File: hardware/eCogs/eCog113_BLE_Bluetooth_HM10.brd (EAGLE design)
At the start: 47.5 x 28 mm, 5 parts

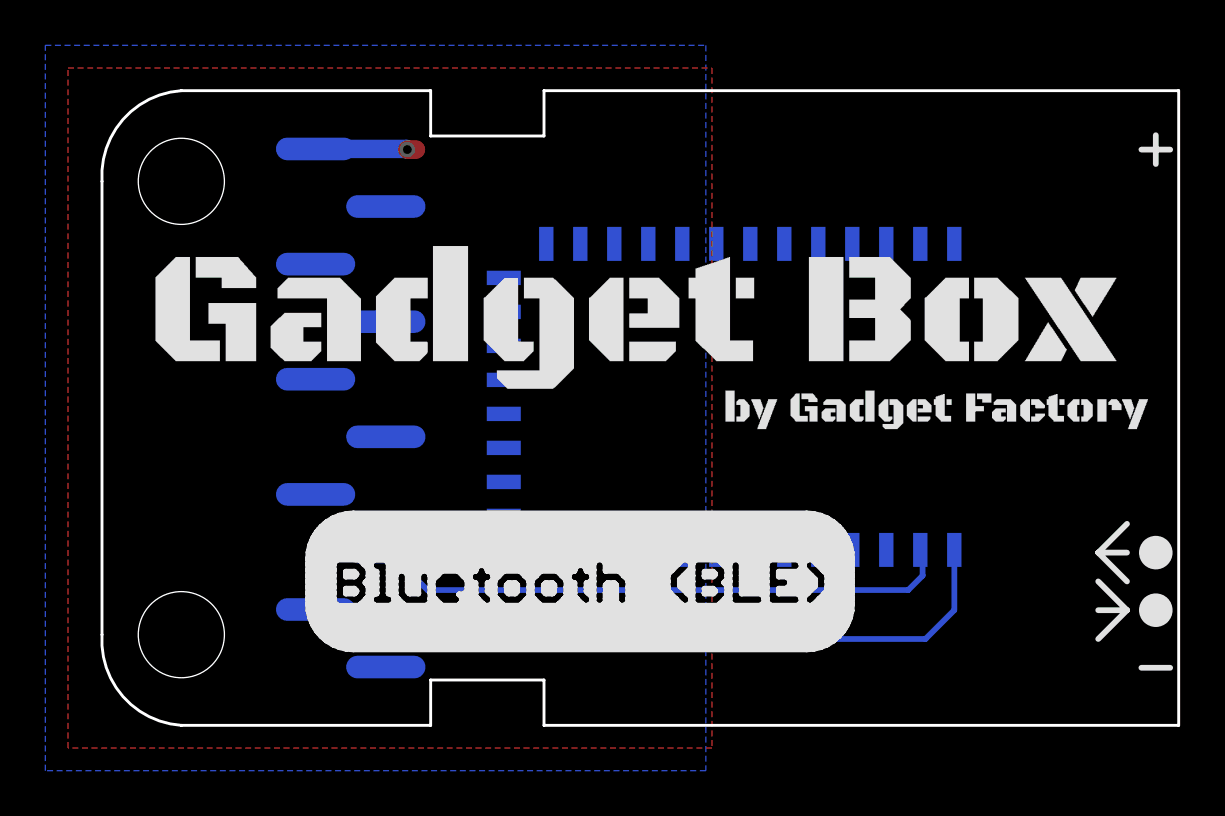
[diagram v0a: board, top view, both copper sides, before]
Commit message: Update eCogs to through hole
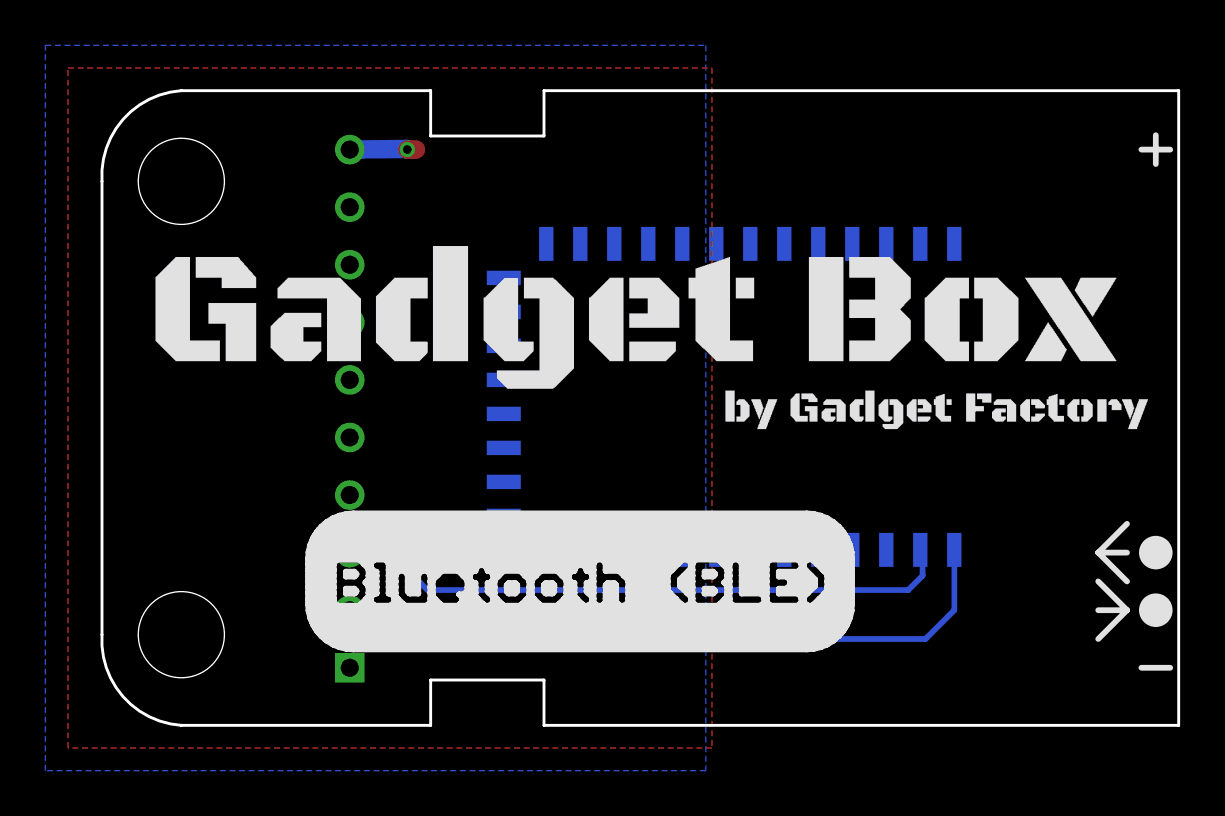
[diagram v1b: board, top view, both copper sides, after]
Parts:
- ECOG: value ECOG_GENERAL_ROWECOG_GENERAL_SMD -> ECOG_GENERAL_ROWTHROUGHOLE; device eCogs:ECOG_GENERAL_SMD -> eCogs:ECOG_GENERAL_TH
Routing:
- net RX/MOSI: track 25.8 -> 27.4 mm
- net 3V3: track 7.62 -> 6.12 mm
- net TX/MISO: track 31.9 -> 30.4 mm
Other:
- board text added: "ecog113 v2.1"
- board text removed: "ecog113 v2.0"
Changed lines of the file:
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@@
 <plain>
 <text x="40.099" y="25.273" size="0.8128" layer="22" font="vector" rot="MR0">ecog113.GadgetFactory.net</text>
-<text x="39.702" y="2.159" size="1.016" layer="22" font="vector" rot="MR0">ecog113 v2.0</text>
+<text x="39.702" y="2.159" size="1.016" layer="22" font="vector" rot="MR0">ecog113 v2.1</text>
 <text x="39.702" y="3.429" size="1.016" layer="22" font="vector" rot="MR0">BLE Bluetooth (HM-10)</text>
 <text x="39.702" y="4.699" size="1.016" layer="22" font="vector" rot="MR0">eCogs</text>
@@
 </autorouter>
 <elements>
-<element name="ECOG" library="eCogs" package="ECOG_GENERAL_SMD" value="ECOG_GENERAL_ROWECOG_GENERAL_SMD" x="0" y="0" smashed="yes">
-<attribute name="DIGIKEY" value="S1013EC-10-ND" x="0" y="0" size="1.778" layer="27" display="off"/>
-</element>
+<element name="ECOG" library="eCogs" package="ECOG_GENERAL_TH" value="ECOG_GENERAL_ROWTHROUGHOLE" x="0" y="0" smashed="yes"/>
 <element name="U$1" library="GadgetFactory" package="GADGETBOX_TEXT" value="" x="24.13" y="17.78"/>
 <element name="U$2" library="eCogs" package="LEGEND_DIO" value="" x="46.99" y="7.62"/>
@@
 <contactref element="E1" pad="11"/>
 <wire x1="21.6" y1="7.74" x2="23.1" y2="7.74" width="0.3048" layer="16"/>
-<wire x1="9.92324375" y1="25.429" x2="13.941" y2="25.429" width="0.8128" layer="16"/>
+<wire x1="11.43" y1="25.4" x2="13.941" y2="25.429" width="0.8128" layer="16"/>
 <wire x1="13.941" y1="25.429" x2="13.97" y2="25.4" width="0.8128" layer="16"/>
 <via x="13.97" y="25.4" extent="1-16" drill="0.381"/>
@@
 <contactref element="E1" pad="2"/>
 <contactref element="ECOG" pad="G1"/>
-<wire x1="13.02204375" y1="7.649" x2="13.179" y2="7.649" width="0.254" layer="16"/>
+<wire x1="11.43" y1="7.62" x2="13.179" y2="7.649" width="0.254" layer="16"/>
 <wire x1="13.179" y1="7.649" x2="14.859" y2="5.969" width="0.254" layer="16"/>
 <wire x1="14.859" y1="5.969" x2="36.068" y2="5.969" width="0.254" layer="16"/>
@@
 <contactref element="E1" pad="1"/>
 <contactref element="ECOG" pad="G0"/>
-<wire x1="9.92324375" y1="5.1110625" x2="12.6689375" y2="5.1110625" width="0.254" layer="16"/>
+<wire x1="11.43" y1="5.08" x2="12.6689375" y2="5.1110625" width="0.254" layer="16"/>
 <wire x1="12.6689375" y1="5.1110625" x2="13.97" y2="3.81" width="0.254" layer="16"/>
 <wire x1="13.97" y1="3.81" x2="36.83" y2="3.81" width="0.254" layer="16"/>
